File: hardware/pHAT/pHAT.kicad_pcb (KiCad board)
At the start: 2 copper layers, 65 x 30 mm, 16 parts, among them P1 Conn_02x20_Odd_Even, U2 HIH6131-021, U3 P82B96

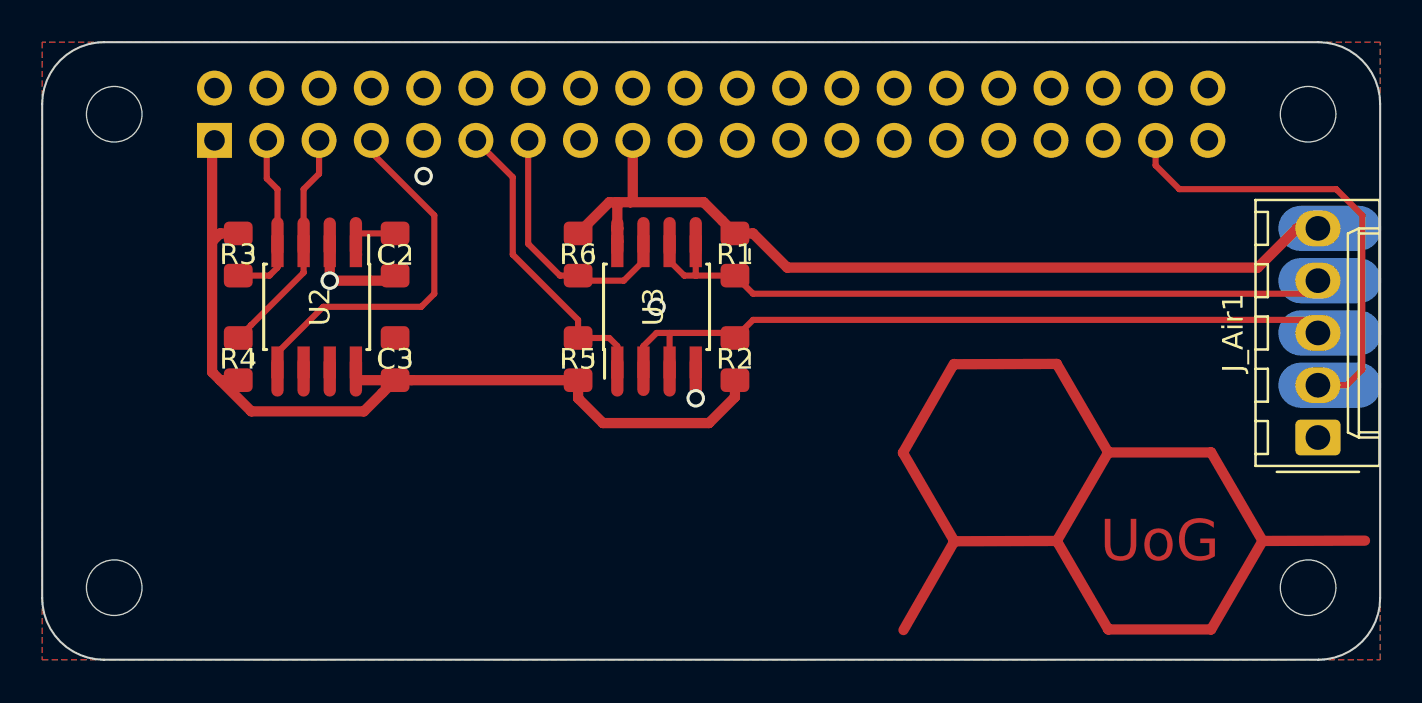
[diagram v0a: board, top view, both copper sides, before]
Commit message: Preparing layout for adding a fan
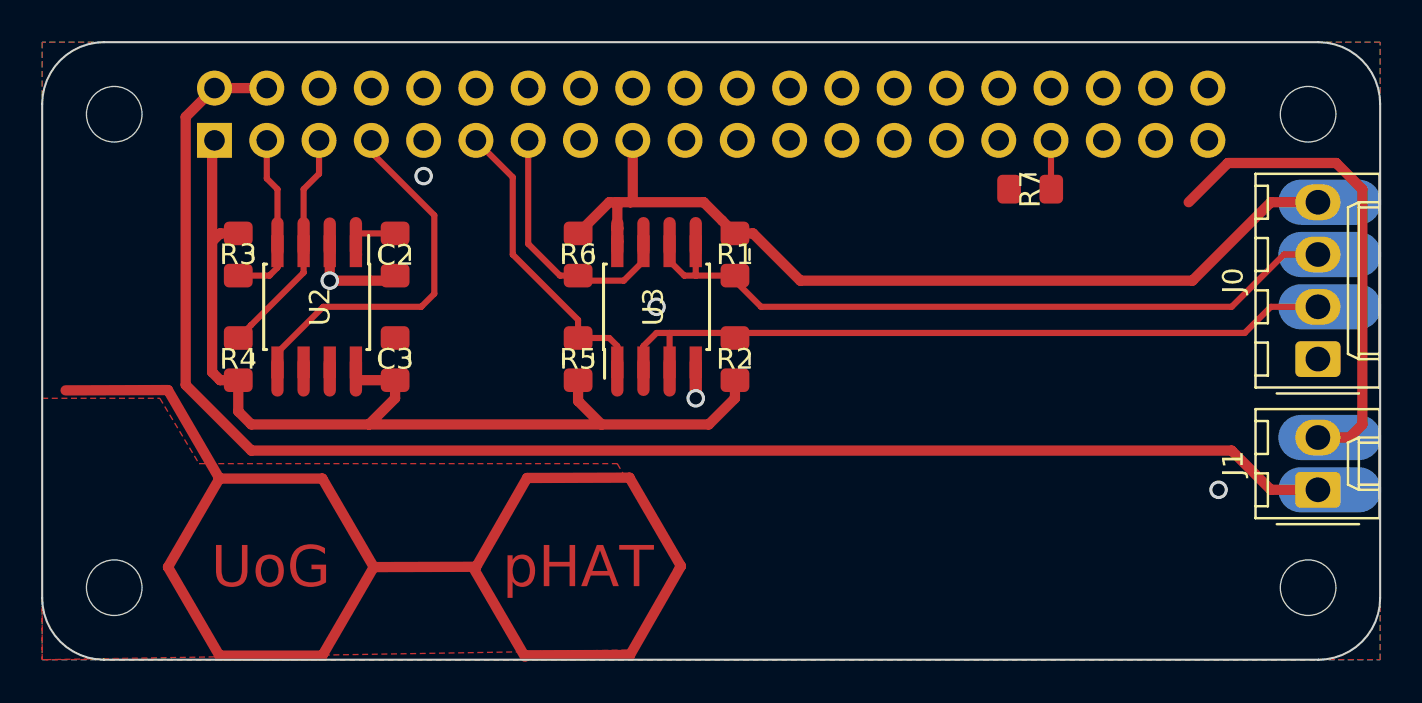
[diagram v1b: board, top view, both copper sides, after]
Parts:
- removed J_Air1: Conn_01x05, Connector_Molex:Molex_KK-254_AE-6410-05A_1x05_P2.54mm_Vertical
- added J0: Conn_01x04, Connector_Molex:Molex_KK-254_AE-6410-04A_1x04_P2.54mm_Vertical, F.Cu at (262.0, 135.4)
- added J1: Conn_01x02, Connector_Molex:Molex_KK-254_AE-6410-02A_1x02_P2.54mm_Vertical, F.Cu at (262.0, 141.7)
- added R7: 5K, Resistor_SMD:R_0805_2012Metric_Pad1.15x1.40mm_HandSolder, F.Cu at (248.0, 127.1)
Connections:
- P1 pad 2: Net-(P1-Pad2) -> +5V
- P1 pad 33: Net-(P1-Pad33) -> /cmd
- P1 pad 37: /alarm_air -> Net-(P1-Pad37)
- P1 pad 4: Net-(P1-Pad4) -> +5V
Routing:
- net +5V: track 0.00 -> 77.5 mm
- net +3V3: track 96.1 -> 155.2 mm
- net (no net): track 64.7 -> 19.9 mm
- net /fan_cmd: track 0.00 -> 26.4 mm
- net /alarm_air: track 25.0 -> 0.00 mm
- net /cmd: track 0.00 -> 2.37 mm
- net /SCLA: track 39.6 -> 40.8 mm
- net GND: vias 4 -> 5
- added copper zone on F.Cu, net (none)
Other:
- rule trace_min: 0.2 -> 0.3
- board text added: "pHAT"

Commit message: Finished fan command circuit (pHAT v3.2)
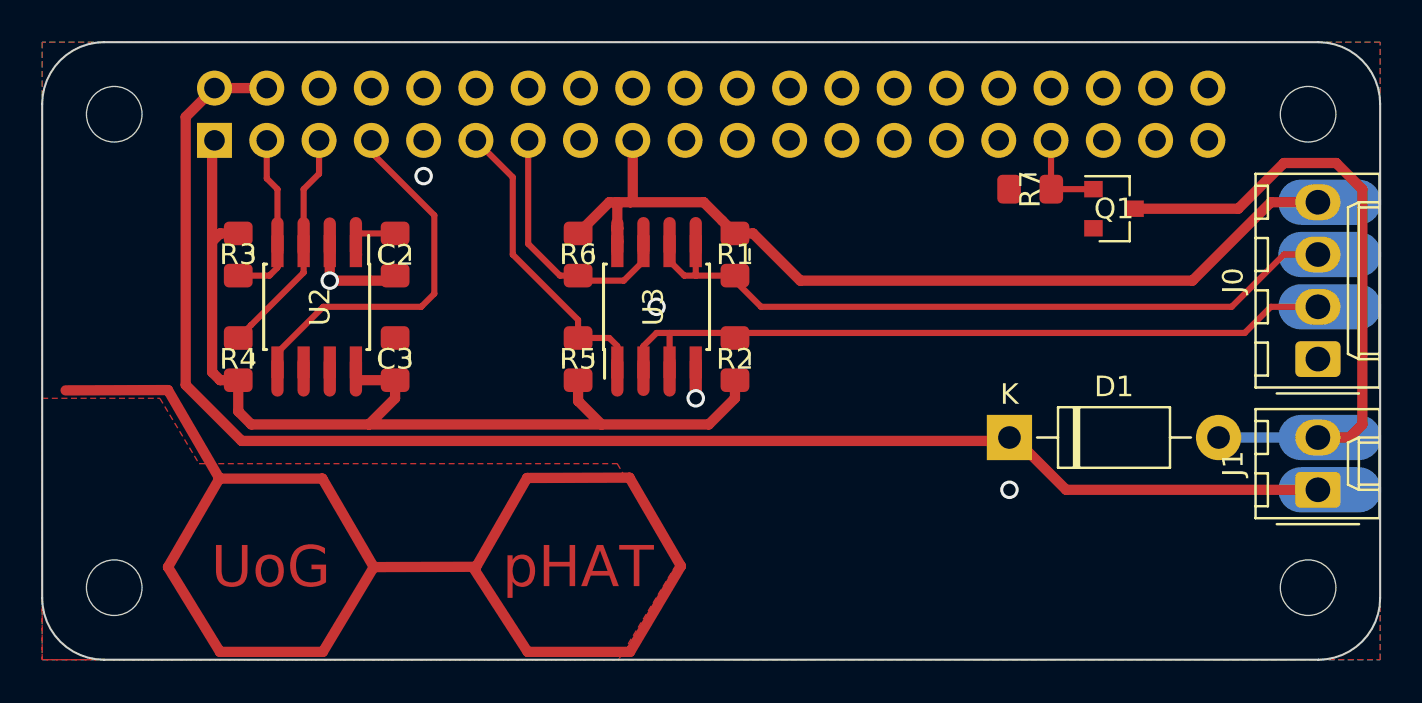
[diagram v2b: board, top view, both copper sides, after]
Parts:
- added D1: 1N4007, Diode_THT:D_DO-41_SOD81_P10.16mm_Horizontal, F.Cu at (247.0, 139.2)
- added Q1: 2N7002, Package_TO_SOT_SMD:SOT-23, F.Cu at (252.1, 128.1)
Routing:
- net /fan_cmd: track 26.4 -> 34.0 mm
- net /cmd: track 2.37 -> 4.42 mm

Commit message: Rework of sensor board and correction of pHAT
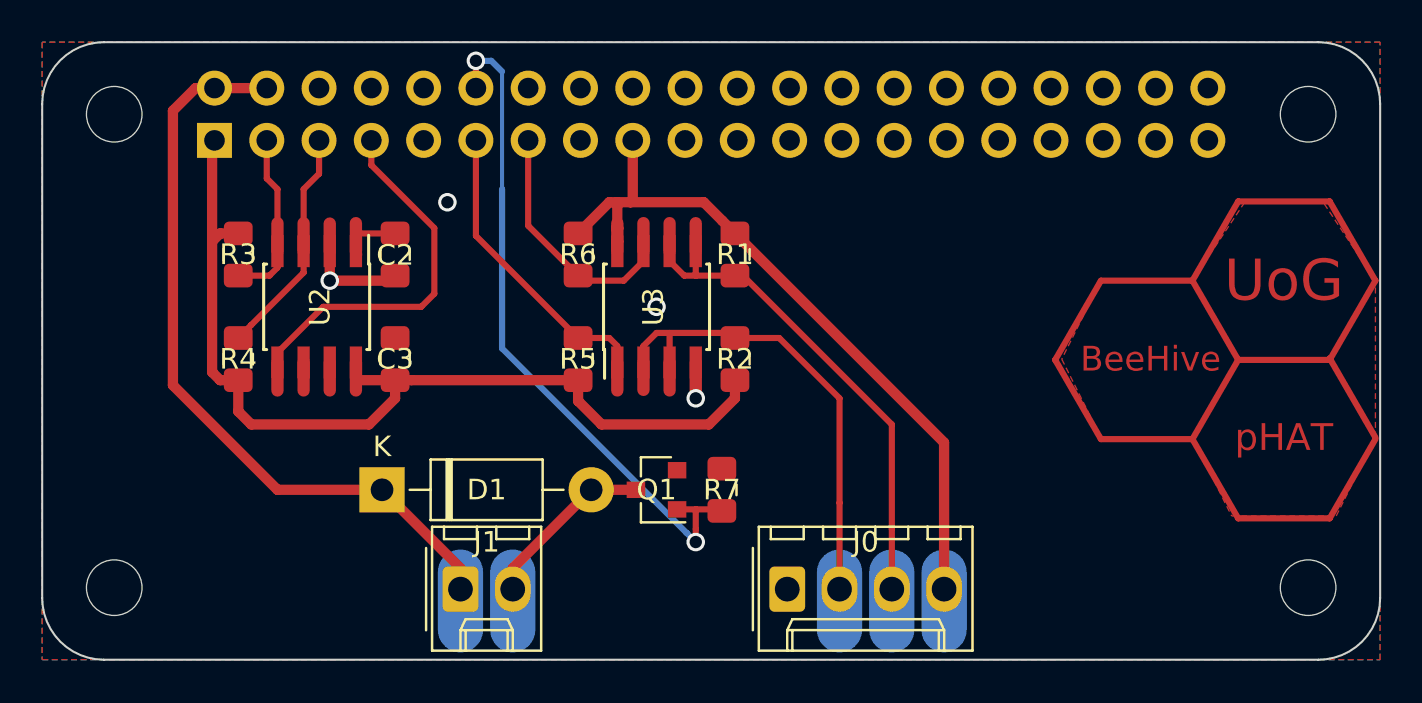
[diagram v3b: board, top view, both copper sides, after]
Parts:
- moved J1 41.9 mm to (220.3, 146.6), turned to 0 degrees
- moved D1 30.6 mm to (216.5, 141.7)
- moved J0 28.1 mm to (236.2, 146.6), turned to 0 degrees
- moved Q1 26.1 mm to (229.8, 141.7), turned to 180 degrees
- moved R7 20.9 mm to (233.0, 141.7), turned to 90 degrees
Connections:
- P1 pad 12: Net-(P1-Pad12) -> /cmd
- P1 pad 33: /cmd -> Net-(P1-Pad33)
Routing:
- net +3V3: track 154.7 -> 88.7 mm
- net (no net): track 19.8 -> 66.7 mm
- net +5V: track 77.6 -> 39.8 mm
- net /cmd: track 4.42 -> 33.4 mm, vias 0 -> 2
- net /fan_cmd: track 34.0 -> 11.4 mm
- net /SDAA: track 42.8 -> 29.5 mm
- net /SCLA: track 40.8 -> 29.3 mm
- net /alarm_hive: track 19.4 -> 19.9 mm
- net /SCL1: track 13.6 -> 13.1 mm
- net GND: vias 5 -> 4
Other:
- net class Default: clearance 0.3 -> 0.2
- rule trace_clearance: 0.3 -> 0.2
- rule trace_min: 0.3 -> 0.2
- board text added: "BeeHive"

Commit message: Polishing the board
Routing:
- net /cmd: track 33.4 -> 67.2 mm, vias 2 -> 0
